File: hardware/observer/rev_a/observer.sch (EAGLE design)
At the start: 27 parts, among them J1 CON_HEADER_2X05-PTH+SHROUDED_A, U1 LPS331AP, U2 MPU-9250, U3 SI1147, U4 SI7021, U5 ATUM

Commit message: mostly routed
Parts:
- removed J2: (no value), pinhead:PINHD-2X2
- added J3: TC2030-CC2538-BL-NL, connector:TC2030-CC2538-BL-NL
- added JP1: (no value), pinhead:PINHD-2X10
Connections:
- removed net 3V3: J1.1
- removed net A7: J2.2
- removed net MOTOR_CTRL: J2.4
- new net !RESET: J3.!RESET, U5.!RESET
- new net AA: JP1.13
- new net BB: JP1.15
- new net BTLDR_CTRL: J3.BL_CTRL, U5.BTLDR_CTRL
- new net BTLDR_RX: J3.RX, U5.BTLDR_RX
- new net BTLDR_TX: J3.TX, U5.BTLDR_TX
- new net CC: JP1.17
- new net UNUSED: U5.C0
- new net UNUSED2: U5.C1
- net !ACCEL_CS: now also JP1.3, U5.B4
- net !BBB_CS: now also JP1.12
- net !PRESSURE_CS: now also JP1.1, U5.B5
- net ACCEL_INT: now also JP1.4, U5.B3
- net BBB_INT: now also JP1.10
- net BBB_MISO: now also JP1.16
- net BBB_MOSI: now also JP1.18
- net BBB_SCLK: now also JP1.14
- net GND: now also J3.GND, JP1.20; no longer J2.1
- net LIGHT_INT: now also JP1.8, U5.C2
- net MISO: now also JP1.5
- net MOSI: now also JP1.6
- net PRESSURE_INT: now also JP1.2, U5.B6
- net SCL: now also JP1.9
- net SCLK: now also JP1.7
- net SDA: now also JP1.11
- net VCC: now also J1.1, J3.VCC, JP1.19; no longer J2.3
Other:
- note removed: "Pin Header"

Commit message: pretty close on the shield board
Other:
- note removed: "Squall Header"
- moved on the sheet: H1, H2, H3, H4, J1, J3, JP1, R4, R5

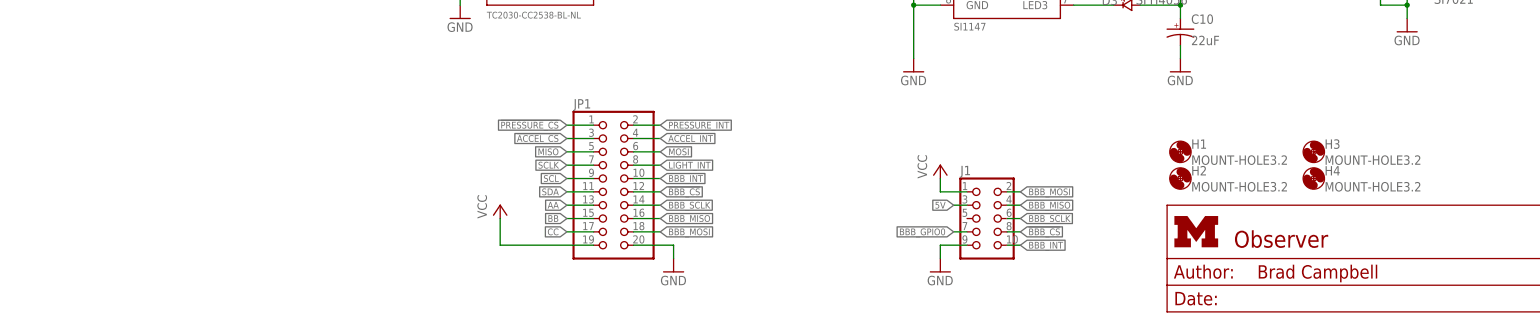
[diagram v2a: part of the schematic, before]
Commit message: new design with mountable sensor board
If the sensor board doesn't need to be attached elsewhere, it can be
attached to the BBB cape.
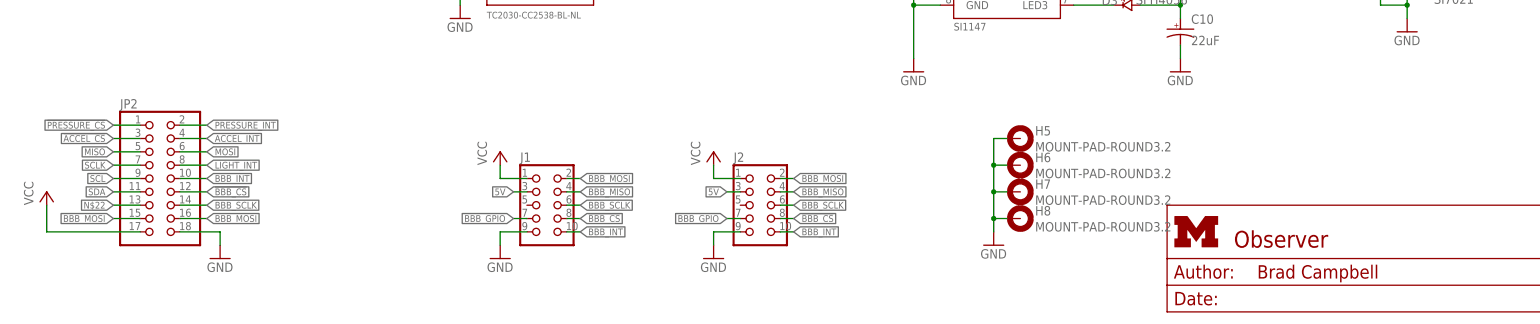
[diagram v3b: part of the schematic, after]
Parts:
- removed H1, H2, H3, H4: MOUNT-HOLE3.2, holes:MOUNT-HOLE3.2
- removed JP1: (no value), pinhead:PINHD-2X10
- added H5, H6, H7, H8: MOUNT-PAD-ROUND3.2, holes:MOUNT-PAD-ROUND3.2
- added J2: CON_HEADER_2X05-SMD+SHROUDED, dp_devices:CON_HEADER_2X05-SMD+SHROUDED
- added JP2: (no value), pinhead:PINHD-2X9
- J1: value CON_HEADER_2X05-PTH+SHROUDED_A -> CON_HEADER_2X05-SMD+SHROUDED; device dp_devices:CON_HEADER_2X05-PTH+SHROUDED_A -> dp_devices:CON_HEADER_2X05-SMD+SHROUDED; DIGIKEY ED1543-ND -> (none)
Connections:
- removed net AA: JP1.13
- removed net BB: JP1.15
- removed net BBB_GPIO0: J1.7
- removed net CC: JP1.17
- new net BBB_GPIO: J1.7, J2.7
- new net N$22: JP2.13
- net !ACCEL_CS: now also JP2.3; no longer JP1.3
- net !BBB_CS: now also J2.8, JP2.12; no longer JP1.12
- net !PRESSURE_CS: now also JP2.1; no longer JP1.1
- net 5V: now also J2.3
- net ACCEL_INT: now also JP2.4; no longer JP1.4
- net BBB_INT: now also J2.10, JP2.10; no longer JP1.10
- net BBB_MISO: now also J2.4; no longer JP1.16
- net BBB_MOSI: now also J2.2, JP2.15, JP2.16; no longer JP1.18
- net BBB_SCLK: now also J2.6, JP2.14; no longer JP1.14
- net GND: now also H5.MOUNT, H6.MOUNT, H7.MOUNT, H8.MOUNT, J2.9, JP2.18; no longer JP1.20
- net LIGHT_INT: now also JP2.8; no longer JP1.8
- net MISO: now also JP2.5; no longer JP1.5
- net MOSI: now also JP2.6; no longer JP1.6
- net PRESSURE_INT: now also JP2.2; no longer JP1.2
- net SCL: now also JP2.9; no longer JP1.9
- net SCLK: now also JP2.7; no longer JP1.7
- net SDA: now also JP2.11; no longer JP1.11
- net VCC: now also J2.1, JP2.17; no longer JP1.19
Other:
- moved on the sheet: J1

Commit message: working on sensor board
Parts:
- removed JP2: (no value), pinhead:PINHD-2X9
- added J4: PINHD-2X6/SMD, headers:PINHD-2X6/SMD
- added U6: AMN41121, chips:AMN41121
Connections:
- removed net N$22: JP2.13
- removed net UNUSED: U5.C0
- removed net UNUSED2: U5.C1
- new net PIR_OUT: U5.B5, U6.OUT
- new net UN: U5.B6
- net !ACCEL_CS: now also J4.8; no longer JP2.3
- net !BBB_CS: now also U5.ADC6; no longer JP2.12, U5.ADC4
- net !PRESSURE_CS: now also J4.1, J4.11, U5.C1; no longer JP2.1, U5.B5
- net ACCEL_INT: now also J4.4; no longer JP2.4
- net BBB_INT: now also U5.ADC7; no longer JP2.10, U5.ADC3
- net BBB_MISO: now also U5.ADC4; no longer U5.ADC6
- net BBB_MOSI: now also U5.ADC3; no longer JP2.15, JP2.16, U5.ADC7
- net BBB_SCLK: no longer JP2.14
- net GND: now also U6.GND; no longer JP2.18
- net LIGHT_INT: now also J4.9; no longer JP2.8
- net MISO: now also J4.5; no longer JP2.5
- net MOSI: now also J4.6; no longer JP2.6
- net PRESSURE_INT: now also J4.12, J4.2, U5.C0; no longer JP2.2, U5.B6
- net SCL: now also J4.3; no longer JP2.9
- net SCLK: now also J4.7; no longer JP2.7
- net SDA: now also J4.10; no longer JP2.11
- net VCC: now also U6.VCC; no longer JP2.17

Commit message: basically done with observer
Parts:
- removed J4: PINHD-2X6/SMD, headers:PINHD-2X6/SMD
- added J5: PINHD-2X8/SMD, headers:PINHD-2X8/SMD
- J1, J2: DIGIKEY (none) -> S9185-ND
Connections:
- new net N$2: J5.3
- new net N$20: J5.4
- new net UNUSED3: J5.6
- net !ACCEL_CS: now also J5.7, U5.B3; no longer J4.8, U5.B4
- net !PRESSURE_CS: now also J5.15; no longer J4.1, J4.11
- net ACCEL_INT: now also J5.8, U5.B4; no longer J4.4, U5.B3
- net GND: now also J5.2
- net LIGHT_INT: now also J5.13; no longer J4.9
- net MISO: now also J5.10; no longer J4.5
- net MOSI: now also J5.9; no longer J4.6
- net PIR_OUT: now also J5.5
- net PRESSURE_INT: now also J5.16; no longer J4.12, J4.2
- net SCL: now also J5.11; no longer J4.3
- net SCLK: now also J5.12; no longer J4.7
- net SDA: now also J5.14; no longer J4.10
- net VCC: now also J5.1
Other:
- note added: "PIR Sensor"
- moved on the sheet: C10, C7, C8, D1, D2, D3, H5, H6, H7, H8, J1, J2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
